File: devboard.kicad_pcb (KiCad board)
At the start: 2 copper layers, 23 x 52 mm, 24 parts, among them J1 USB4105-GF-A, J2 Conn_01x08_Pin, J3 Conn_01x08_Pin, U1 STM32F411CEU6, U2 AP2120N-3.3TRG1, U3 USBLC6-2SC6Y

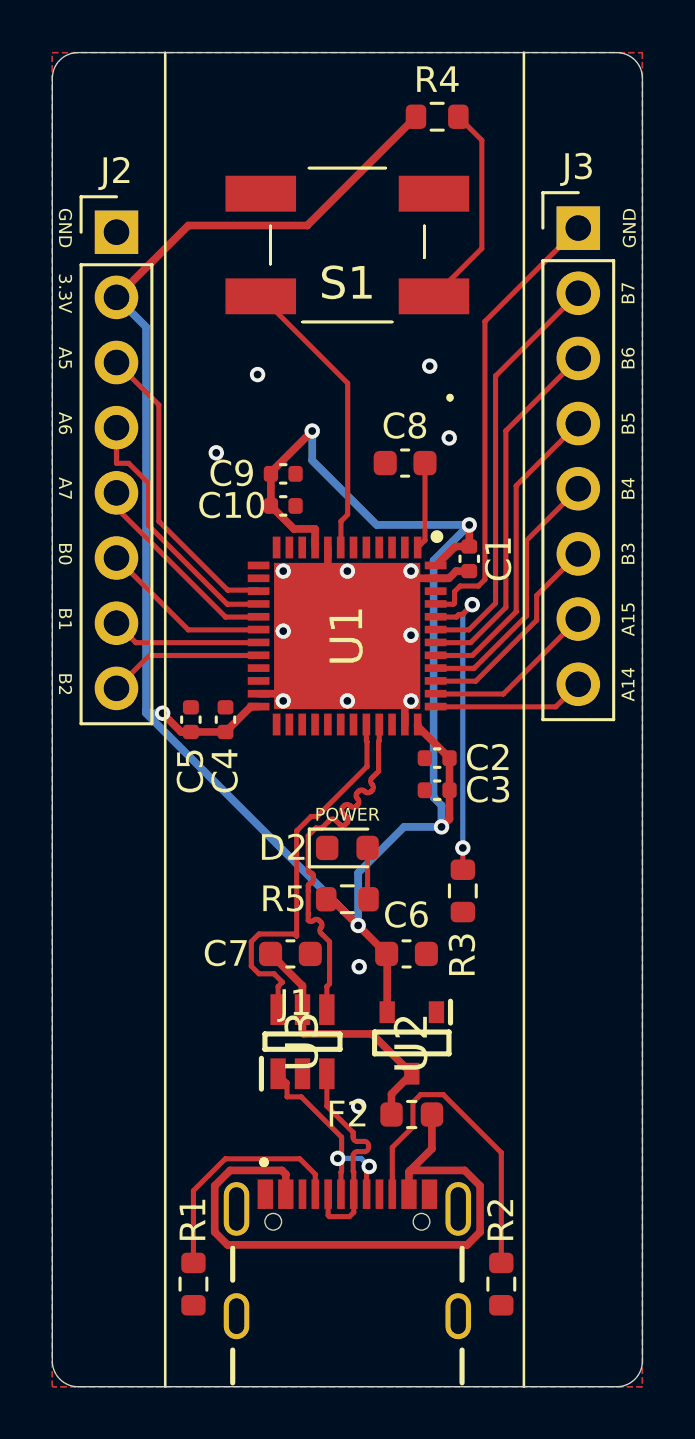
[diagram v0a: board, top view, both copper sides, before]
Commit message: Ground connections fixes
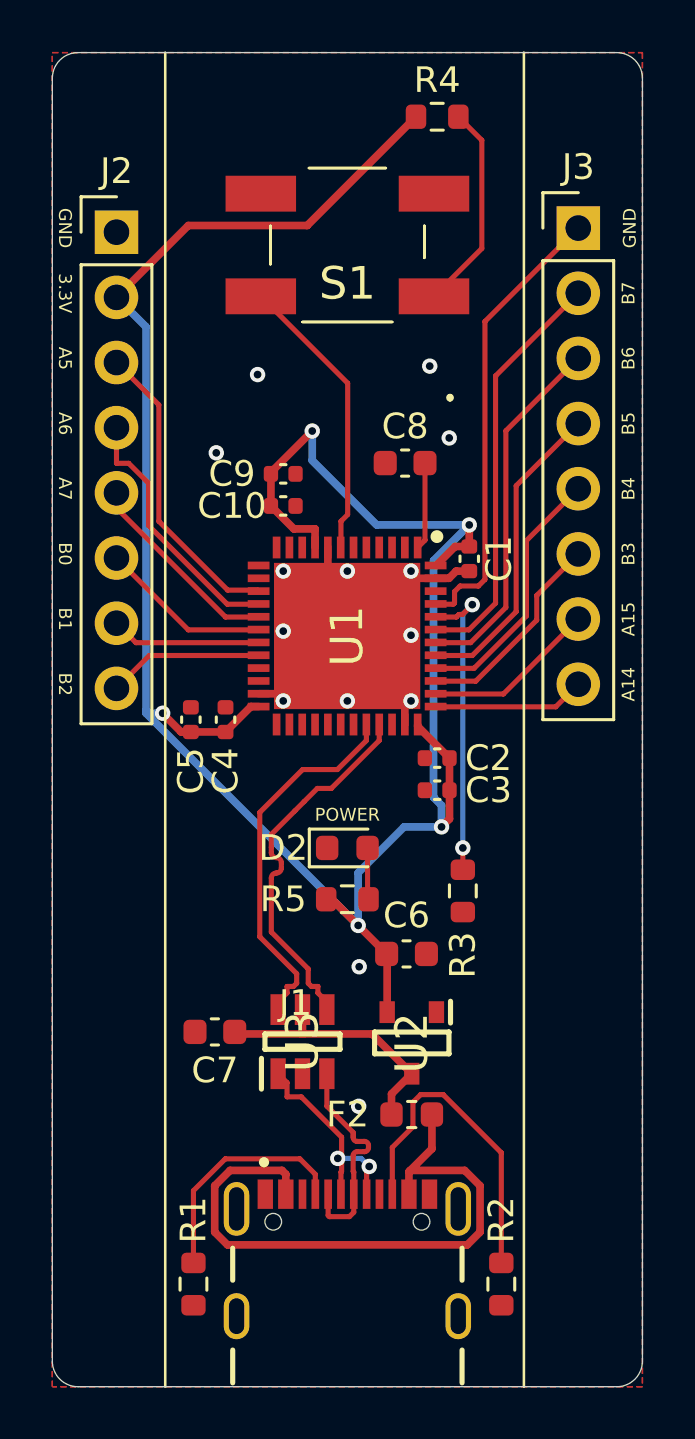
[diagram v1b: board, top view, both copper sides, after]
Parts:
- moved C7 4.23 mm to (108.3, 111.2), turned to 180 degrees

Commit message: Fixed ALL DRC and unconnected errors
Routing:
- net GND: track 18.3 -> 26.6 mm, vias 14 -> 15
- net Net-(F2-Pad2): track 24.7 -> 28.2 mm
- net D-: track 8.65 -> 10.2 mm

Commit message: Fixes
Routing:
- net GND: vias 15 -> 17
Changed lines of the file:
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@@
+	)
+	(via
+		(at 118.19 115.72)
+		(size 0.6)
+		(drill 0.3)
+		(layers "F.Cu" "B.Cu")
+		(free yes)
+		(net 33)
 	)
 	(via
@@
 		(net 33)
 	)
+	(via
+		(at 113.9 112.65)
+		(size 0.6)
+		(drill 0.3)
+		(layers "F.Cu" "B.Cu")
+		(free yes)
+		(net 33)
+	)

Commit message: Fixes
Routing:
- net GND: vias 17 -> 31
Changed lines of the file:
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@@
 			(outputformat 1)
 			(mirror no)
-			(drillshape 1)
+			(drillshape 0)
 			(scaleselection 1)
-			(outputdirectory "")
+			(outputdirectory "gerber/")
 		)
 	)
@@
 	)
 	(via
-		(at 108.39 88.6)
+		(at 114.84 101.6)
+		(size 0.6)
+		(drill 0.3)
+		(layers "F.Cu" "B.Cu")
+		(free yes)
+		(net 33)
+	)
+	(via
+		(at 107.29 88.99)
+		(size 0.6)
+		(drill 0.3)
+		(layers "F.Cu" "B.Cu")
+		(free yes)
+		(net 33)
+	)
+	(via
+		(at 117.97 88.18)
 		(size 0.6)
 		(drill 0.3)
@@
 	)
 	(via
-		(at 116.71 85.22)
+		(at 114.43 80.48)
+		(size 0.6)
+		(drill 0.3)
+		(layers "F.Cu" "B.Cu")
+		(free yes)
+		(net 33)
+	)
+	(via
+		(at 114.26 84.47)
 		(size 0.6)
 		(drill 0.3)
@@
 	)
 	(via
+		(at 107.42 84.54)
+		(size 0.6)
+		(drill 0.3)
+		(layers "F.Cu" "B.Cu")
+		(free yes)
+		(net 33)
+	)
+	(via
+		(at 107.84 97.28)
+		(size 0.6)
+		(drill 0.3)
+		(layers "F.Cu" "B.Cu")
+		(free yes)
+		(net 33)
+	)
+	(via
+		(at 104.27 115.09)
+		(size 0.6)
+		(drill 0.3)
+		(layers "F.Cu" "B.Cu")
+		(free yes)
+		(net 33)
+	)
+	(via
+		(at 123.18 104.09)
+		(size 0.6)
+		(drill 0.3)
+		(layers "F.Cu" "B.Cu")
+		(free yes)
+		(net 33)
+	)
+	(via
 		(at 113.5 120)
 		(size 0.6)
@@
 	)
 	(via
+		(at 122.75 74.59)
+		(size 0.6)
+		(drill 0.3)
+		(layers "F.Cu" "B.Cu")
+		(free yes)
+		(net 33)
+	)
+	(via
+		(at 116.21 105.07)
+		(size 0.6)
+		(drill 0.3)
+		(layers "F.Cu" "B.Cu")
+		(free yes)
+		(net 33)
+	)
+	(via
 		(at 113.5 98.27)
 		(size 0.6)
@@
 	)
 	(via
+		(at 104.78 106.17)
+		(size 0.6)
+		(drill 0.3)
+		(layers "F.Cu" "B.Cu")
+		(free yes)
+		(net 33)
+	)
+	(via
 		(at 113.5 93.21)
 		(size 0.6)
@@
 	)
 	(via
+		(at 111.99 107.47)
+		(size 0.6)
+		(drill 0.3)
+		(layers "F.Cu" "B.Cu")
+		(free yes)
+		(net 33)
+	)
+	(via
 		(at 115.98 95.71)
 		(size 0.6)
@@
 	)
 	(via
+		(at 104.1 74.86)
+		(size 0.6)
+		(drill 0.3)
+		(layers "F.Cu" "B.Cu")
+		(free yes)
+		(net 33)
+	)
+	(via
 		(at 111 98.27)
 		(size 0.6)
@@
 	)
 	(via
+		(at 111.77 103.09)
+		(size 0.6)
+		(drill 0.3)
+		(layers "F.Cu" "B.Cu")
+		(free yes)
+		(net 33)
+	)
+	(via
 		(at 110 85.55)
 		(size 0.6)
@@
 	)
 	(via
-		(at 117.47 88.02)
+		(at 116.09 85.51)
+		(size 0.6)
+		(drill 0.3)
+		(layers "F.Cu" "B.Cu")
+		(free yes)
+		(net 33)
+	)
+	(via
+		(at 122.82 117.58)
 		(size 0.6)
 		(drill 0.3)

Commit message: Fix VBAT
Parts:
- C8: value 2.2 uF -> 100 nF
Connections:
- C8 pad 2: Net-(U1-VBAT) -> +3.3V
- U1 pad 1: Net-(U1-VBAT) -> +3.3V
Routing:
- net Net-(U1-VBAT): track 3.41 -> 0.00 mm
- net +3.3V: track 94.1 -> 97.5 mm, vias 5 -> 6
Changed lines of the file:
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@@
 	(net 34 "Net-(J1-CC2)")
 	(net 35 "unconnected-(J1-SBU1-PadA8)")
-	(net 36 "Net-(U1-VBAT)")
-	(net 37 "Net-(U1-BOOT0)")
-	(net 38 "NRST")
-	(net 39 "B9")
-	(net 40 "unconnected-(U1-PH0-OSC_OUT-Pad6)")
-	(net 41 "unconnected-(U1-PC13-Pad2)")
-	(net 42 "B13")
-	(net 43 "B12")
-	(net 44 "unconnected-(U1-VCAP_1-Pad22)")
-	(net 45 "unconnected-(U1-PC14-OSC32_IN-Pad3)")
-	(net 46 "B10")
-	(net 47 "B14")
-	(net 48 "unconnected-(U1-PH0-OSC_IN-Pad5)")
-	(net 49 "unconnected-(U1-PC15-OSC32_OUT-Pad4)")
-	(net 50 "B15")
-	(net 51 "Net-(D2-A)")
-	(net 52 "Net-(S1-COM_1)")
+	(net 36 "Net-(U1-BOOT0)")
+	(net 37 "NRST")
+	(net 38 "B9")
+	(net 39 "unconnected-(U1-PH0-OSC_OUT-Pad6)")
+	(net 40 "unconnected-(U1-PC13-Pad2)")
+	(net 41 "B13")
+	(net 42 "B12")
+	(net 43 "unconnected-(U1-VCAP_1-Pad22)")
+	(net 44 "unconnected-(U1-PC14-OSC32_IN-Pad3)")
+	(net 45 "B10")
+	(net 46 "B14")
+	(net 47 "unconnected-(U1-PH0-OSC_IN-Pad5)")
+	(net 48 "unconnected-(U1-PC15-OSC32_OUT-Pad4)")
+	(net 49 "B15")
+	(net 50 "Net-(D2-A)")
+	(net 51 "Net-(S1-COM_1)")
 	(footprint "Capacitor_SMD:C_0603_1608Metric"
 		(layer "F.Cu")
@@
 			(layers "F.Cu" "F.Mask" "F.Paste")
 			(roundrect_rratio 0.25)
-			(net 52 "Net-(S1-COM_1)")
+			(net 51 "Net-(S1-COM_1)")
 			(pintype "passive")
 		)
@@
 			)
 		)
-		(property "Value" "2.2 uF"
+		(property "Value" "100 nF"
 			(at 0 1.43 0)
 			(layer "F.Fab")
@@
 			(layers "F.Cu" "F.Mask" "F.Paste")
 			(roundrect_rratio 0.25)
-			(net 36 "Net-(U1-VBAT)")
+			(net 30 "+3.3V")
 			(pintype "passive")
 		)
@@
 			(layers "F.Cu" "F.Mask" "F.Paste")
 			(roundrect_rratio 0.25)
-			(net 51 "Net-(D2-A)")
+			(net 50 "Net-(D2-A)")
 			(pinfunction "A")
 			(pintype "passive")
@@
 			(size 1.4 2.75)
 			(layers "F.Cu" "F.Mask" "F.Paste")
-			(net 52 "Net-(S1-COM_1)")
+			(net 51 "Net-(S1-COM_1)")
 			(pinfunction "COM_1")
 			(pintype "passive")
@@
 			(size 1.4 2.75)
 			(layers "F.Cu" "F.Mask" "F.Paste")
-			(net 38 "NRST")
+			(net 37 "NRST")
 			(pinfunction "COM_2")
 			(pintype "passive")
@@
 			(layers "F.Cu" "F.Mask" "F.Paste")
 			(roundrect_rratio 0.25)
-			(net 51 "Net-(D2-A)")
+			(net 50 "Net-(D2-A)")
 			(pintype "passive")
 		)
@@
 			(size 0.3 0.85)
 			(layers "F.Cu" "F.Mask" "F.Paste")
-			(net 36 "Net-(U1-VBAT)")
+			(net 30 "+3.3V")
 			(pinfunction "VBAT")
 			(pintype "passive")
@@
 			(size 0.3 0.85)
 			(layers "F.Cu" "F.Mask" "F.Paste")
-			(net 41 "unconnected-(U1-PC13-Pad2)")
+			(net 40 "unconnected-(U1-PC13-Pad2)")
 			(pinfunction "PC13")
 			(pintype "passive+no_connect")
@@
 			(size 0.3 0.85)
 			(layers "F.Cu" "F.Mask" "F.Paste")
-			(net 45 "unconnected-(U1-PC14-OSC32_IN-Pad3)")
+			(net 44 "unconnected-(U1-PC14-OSC32_IN-Pad3)")
 			(pinfunction "PC14-OSC32_IN")
 			(pintype "passive+no_connect")
@@
 			(size 0.3 0.85)
 			(layers "F.Cu" "F.Mask" "F.Paste")
-			(net 49 "unconnected-(U1-PC15-OSC32_OUT-Pad4)")
+			(net 48 "unconnected-(U1-PC15-OSC32_OUT-Pad4)")
 			(pinfunction "PC15-OSC32_OUT")
 			(pintype "passive+no_connect")
@@
 			(size 0.3 0.85)
 			(layers "F.Cu" "F.Mask" "F.Paste")
-			(net 48 "unconnected-(U1-PH0-OSC_IN-Pad5)")
+			(net 47 "unconnected-(U1-PH0-OSC_IN-Pad5)")
 			(pinfunction "PH0-OSC_IN")
 			(pintype "passive+no_connect")
@@
 			(size 0.3 0.85)
 			(layers "F.Cu" "F.Mask" "F.Paste")
-			(net 40 "unconnected-(U1-PH0-OSC_OUT-Pad6)")
+			(net 39 "unconnected-(U1-PH0-OSC_OUT-Pad6)")
 			(pinfunction "PH0-OSC_OUT")
 			(pintype "passive+no_connect")
@@
 			(size 0.3 0.85)
 			(layers "F.Cu" "F.Mask" "F.Paste")
-			(net 38 "NRST")
+			(net 37 "NRST")
 			(pinfunction "NRST")
 			(pintype "passive")
@@
 			(size 0.3 0.85)
 			(layers "F.Cu" "F.Mask" "F.Paste")
-			(net 46 "B10")
+			(net 45 "B10")
 			(pinfunction "PB10")
 			(pintype "passive+no_connect")
@@
 			(size 0.3 0.85)
 			(layers "F.Cu" "F.Mask" "F.Paste")
-			(net 44 "unconnected-(U1-VCAP_1-Pad22)")
+			(net 43 "unconnected-(U1-VCAP_1-Pad22)")
 			(pinfunction "VCAP_1")
 			(pintype "passive+no_connect")
@@
 			(size 0.3 0.85)
 			(layers "F.Cu" "F.Mask" "F.Paste")
-			(net 43 "B12")
+			(net 42 "B12")
 			(pinfunction "PB12")
 			(pintype "passive+no_connect")
@@
 			(size 0.3 0.85)
 			(layers "F.Cu" "F.Mask" "F.Paste")
-			(net 42 "B13")
+			(net 41 "B13")
 			(pinfunction "PB13")
 			(pintype "passive+no_connect")
@@
 			(size 0.3 0.85)
 			(layers "F.Cu" "F.Mask" "F.Paste")
-			(net 47 "B14")
+			(net 46 "B14")
 			(pinfunction "PB14")
 			(pintype "passive+no_connect")
@@
 			(size 0.3 0.85)
 			(layers "F.Cu" "F.Mask" "F.Paste")
-			(net 50 "B15")
+			(net 49 "B15")
 			(pinfunction "PB15")
 			(pintype "passive+no_connect")
@@
 			(size 0.3 0.85)
 			(layers "F.Cu" "F.Mask" "F.Paste")
-			(net 37 "Net-(U1-BOOT0)")
+			(net 36 "Net-(U1-BOOT0)")
 			(pinfunction "BOOT0")
 			(pintype "passive")
@@
 			(size 0.3 0.85)
 			(layers "F.Cu" "F.Mask" "F.Paste")
-			(net 39 "B9")
+			(net 38 "B9")
 			(pinfunction "PB9")
 			(pintype "passive+no_connect")
@@
 			(layers "F.Cu" "F.Mask" "F.Paste")
 			(roundrect_rratio 0.25)
-			(net 37 "Net-(U1-BOOT0)")
+			(net 36 "Net-(U1-BOOT0)")
 			(pintype "passive")
 		)
@@
 	)
 	(segment
+		(start 116.525 92.005)
+		(end 116.24 92.29)
+		(width 0.3)
+		(layer "F.Cu")
+		(net 30)
+	)
+	(segment
 		(start 115.05 108.15)
 		(end 115.03 108.13)
@@
 	)
 	(segment
+		(start 116.525 89)
+		(end 116.525 91.4)
+		(width 0.3)
+		(layer "F.Cu")
+		(net 30)
+	)
+	(segment
+		(start 116.525 91.4)
+		(end 116.525 92.005)
+		(width 0.3)
+		(layer "F.Cu")
+		(net 30)
+	)
+	(segment
 		(start 115.05 110.4)
 		(end 115.05 108.15)
@@
 		(net 30)
 	)
+	(via
+		(at 116.525 91.4)
+		(size 0.6)
+		(drill 0.3)
+		(layers "F.Cu" "B.Cu")
+		(net 30)
+	)
 	(segment
 		(start 106.3 98.75)
@@
 	)
 	(segment
-		(start 116.525 92.005)
-		(end 116.24 92.29)
-		(width 0.2)
-		(layer "F.Cu")
-		(net 36)
-	)
-	(segment
-		(start 116.525 89)
-		(end 116.525 92.005)
-		(width 0.2)
-		(layer "F.Cu")
-		(net 36)
-	)
-	(segment
 		(start 117.85 94.9)
 		(end 117.75 95)
 		(width 0.2)
 		(layer "F.Cu")
-		(net 37)
+		(net 36)
 	)
 	(segment
@@
 		(width 0.2)
 		(layer "F.Cu")
-		(net 37)
+		(net 36)
 	)
 	(segment
@@
 		(width 0.2)
 		(layer "F.Cu")
-		(net 37)
+		(net 36)
 	)
 	(segment
@@
 		(width 0.2)
 		(layer "F.Cu")
-		(net 37)
+		(net 36)
 	)
 	(segment
@@
 		(width 0.2)
 		(layer "F.Cu")
-		(net 37)
+		(net 36)
 	)
 	(via
@@
 		(drill 0.3)
 		(layers "F.Cu" "B.Cu")
-		(net 37)
+		(net 36)
 	)
 	(via
@@
 		(drill 0.3)
 		(layers "F.Cu" "B.Cu")
-		(net 37)
+		(net 36)
 	)
 	(segment
@@
 		(width 0.2)
 		(layer "B.Cu")
-		(net 37)
+		(net 36)
 	)
 	(segment
@@
 		(width 0.2)
 		(layer "B.Cu")
-		(net 37)
+		(net 36)
 	)
 	(segment
@@
 		(width 0.2)
 		(layer "F.Cu")
-		(net 38)
+		(net 37)
 	)
 	(segment
@@
 		(width 0.2)
 		(layer "F.Cu")
-		(net 38)
+		(net 37)
 	)
 	(segment
@@
 		(width 0.2)
 		(layer "F.Cu")
-		(net 38)
+		(net 37)
 	)
 	(segment
@@
 		(width 0.2)
 		(layer "F.Cu")
-		(net 38)
+		(net 37)
 	)
 	(segment
@@
 		(width 0.2)
 		(layer "F.Cu")
-		(net 51)
+		(net 50)
 	)
 	(segment
@@
 		(width 0.2)
 		(layer "F.Cu")
-		(net 51)
+		(net 50)
 	)
 	(segment
@@
 		(width 0.2)
 		(layer "F.Cu")
-		(net 52)
+		(net 51)
 	)
 	(segment
@@
 		(width 0.2)
 		(layer "F.Cu")
-		(net 52)
+		(net 51)
 	)
 	(segment
@@
 		(width 0.2)
 		(layer "F.Cu")
-		(net 52)
+		(net 51)
 	)
 	(zone

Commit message: Fixes
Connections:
- U3 pad 1: D+ -> D-
- U3 pad 3: D- -> D+
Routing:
- net Net-(F2-Pad2): track 28.2 -> 10.2 mm
- net D-: track 10.2 -> 8.09 mm
- net D+: track 8.64 -> 8.05 mm, vias 2 -> 0

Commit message: Fixes
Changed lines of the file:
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@@
-		(net 33)
-		(net_name "GND")
-		(layer "F.Cu")
-		(hatch edge 0.5)
-		(connect_pads
-			(clearance 0.5)
-		)
-		(min_thickness 0.25)
-		(filled_areas_thickness no)
-		(fill yes
-			(thermal_gap 0.5)
-			(thermal_bridge_width 0.5)
-		)
-		(polygon
-			(pts
-				(xy 102 73) (xy 125 73) (xy 125 125) (xy 102 125)
-			)
-		)
-	)
-	(zone
 		(net 33)
 		(net_name "GND")

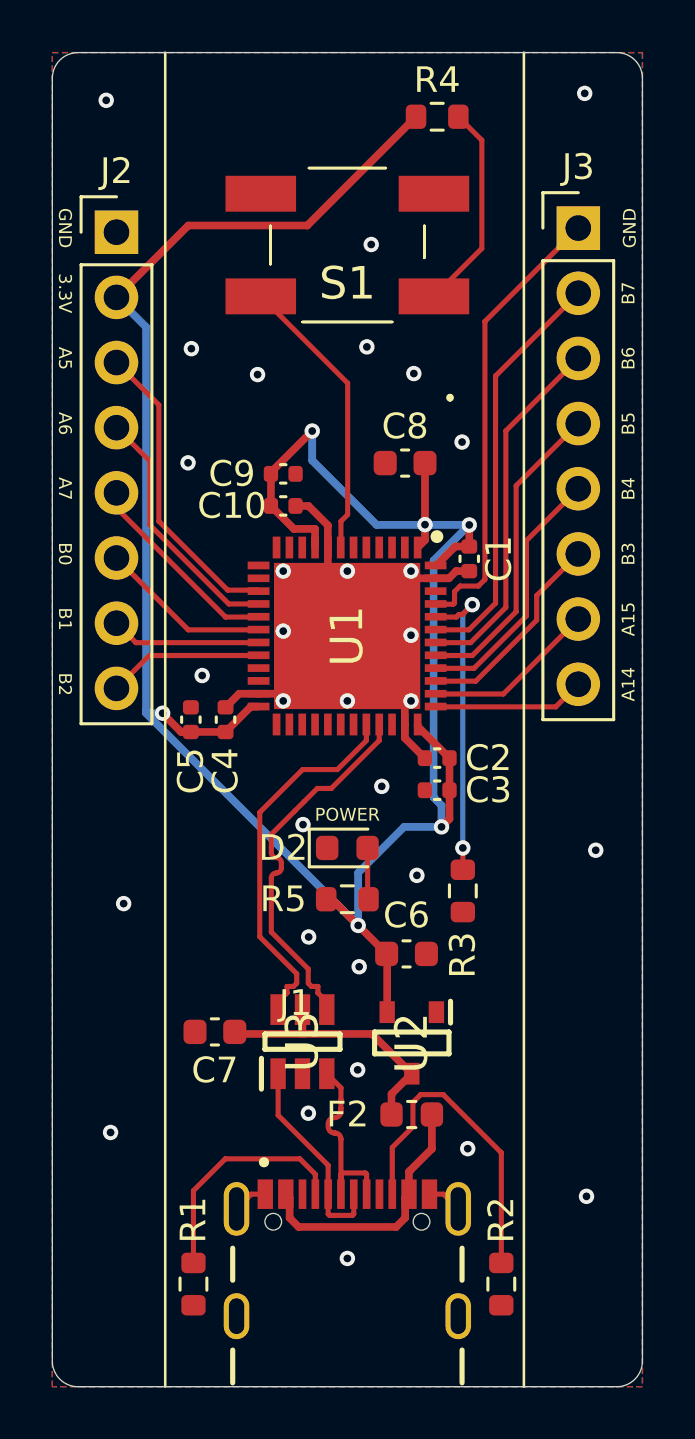
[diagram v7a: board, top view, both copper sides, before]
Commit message: Increase PWR LED resistence value + better silkscreen placement
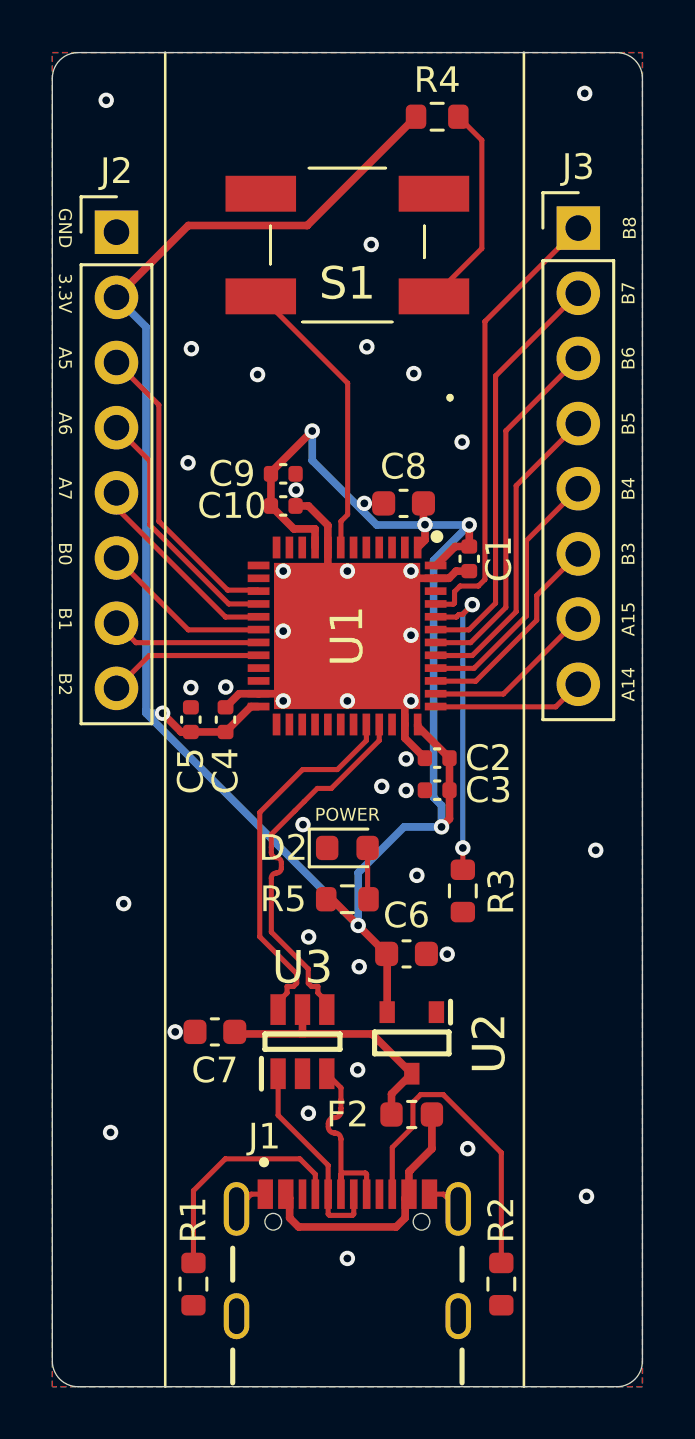
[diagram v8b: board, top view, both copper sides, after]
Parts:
- moved C8 1.57 mm to (115.7, 90.6)
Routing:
- net +3.3V: track 97.5 -> 95.9 mm
- net GND: vias 31 -> 38
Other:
- board text added: "B8"
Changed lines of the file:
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@@
 			(crossoutdnponfab yes)
 			(subtractmaskfromsilk no)
-			(outputformat 4)
+			(outputformat 1)
 			(mirror no)
 			(drillshape 0)
@@
 	(footprint "Capacitor_SMD:C_0603_1608Metric"
 		(layer "F.Cu")
-		(at 115.75 89)
+		(at 115.69 90.57)
 		(descr "Capacitor SMD 0603 (1608 Metric), square (rectangular) end terminal, IPC-7351 nominal, (Body size source: IPC-SM-782 page 76, https://www.pcb-3d.com/wordpress/wp-content/uploads/ipc-sm-782a_amendment_1_and_2.pdf), generated with kicad-footprint-generator")
 		(tags "capacitor")
@@
 		(tags "Diode")
 		(property "Reference" "U3"
-			(at 0 0 90)
+			(at 2.89 0 180)
 			(layer "F.SilkS")
 			(effects
@@
 		)
 		(fp_text user "${REFERENCE}"
-			(at 0 0 90)
+			(at 3.09 -2.66 90)
 			(layer "F.Fab")
 			(effects
@@
 		(tags "Integrated Circuit")
 		(property "Reference" "U2"
-			(at 0 0 270)
+			(at 0.02 -3.02 270)
 			(layer "F.SilkS")
 			(effects
@@
 		)
 		(fp_text user "${REFERENCE}"
-			(at 0 0 270)
+			(at -1.06 -3.02 270)
 			(layer "F.Fab")
 			(effects
@@
 		(tags "resistor")
 		(property "Reference" "R3"
-			(at -2.5 0 90)
+			(at -0.025 1.5 90)
 			(layer "F.SilkS")
 			(effects
@@
 		(at 113.5 122.25)
 		(property "Reference" "J1"
-			(at -2.025 -12.205 0)
+			(at -3.23 -7 0)
 			(layer "F.SilkS")
 			(effects
@@
 		)
 	)
-	(gr_text "GND\n"
+	(gr_text "B8\n"
 		(at 124.8 79.84 90)
 		(layer "F.SilkS")
@@
 	)
 	(segment
+		(start 116.465 90.57)
+		(end 116.465 91.34)
+		(width 0.3)
+		(layer "F.Cu")
+		(net 30)
+	)
+	(segment
 		(start 112.24 91.565)
 		(end 111.415 91.565)
@@
 	)
 	(segment
+		(start 116.465 91.34)
+		(end 116.525 91.4)
+		(width 0.3)
+		(layer "F.Cu")
+		(net 30)
+	)
+	(segment
 		(start 112.675 106)
 		(end 112.9 106)
@@
 	)
 	(segment
-		(start 116.525 89)
-		(end 116.525 91.4)
-		(width 0.3)
-		(layer "F.Cu")
-		(net 30)
-	)
-	(segment
 		(start 116.525 91.4)
 		(end 116.525 92.005)
@@
 	)
 	(via
+		(at 108.76 97.73)
+		(size 0.6)
+		(drill 0.3)
+		(layers "F.Cu" "B.Cu")
+		(free yes)
+		(net 33)
+	)
+	(via
 		(at 118.19 115.72)
 		(size 0.6)
@@
 	)
 	(via
+		(at 115.79 101.76)
+		(size 0.6)
+		(drill 0.3)
+		(layers "F.Cu" "B.Cu")
+		(free yes)
+		(net 33)
+	)
+	(via
+		(at 114.16 90.57)
+		(size 0.6)
+		(drill 0.3)
+		(layers "F.Cu" "B.Cu")
+		(free yes)
+		(net 33)
+	)
+	(via
 		(at 114.26 84.47)
 		(size 0.6)
@@
 	)
 	(via
-		(at 107.84 97.28)
+		(at 117.39 108.14)
+		(size 0.6)
+		(drill 0.3)
+		(layers "F.Cu" "B.Cu")
+		(free yes)
+		(net 33)
+	)
+	(via
+		(at 107.4 97.75)
 		(size 0.6)
 		(drill 0.3)
@@
 	)
 	(via
+		(at 111.5 90.05)
+		(size 0.6)
+		(drill 0.3)
+		(layers "F.Cu" "B.Cu")
+		(free yes)
+		(net 33)
+	)
+	(via
 		(at 123.18 104.09)
 		(size 0.6)
@@
 	)
 	(via
+		(at 115.79 100.53)
+		(size 0.6)
+		(drill 0.3)
+		(layers "F.Cu" "B.Cu")
+		(free yes)
+		(net 33)
+	)
+	(via
 		(at 111.99 107.47)
 		(size 0.6)
@@
 		(size 0.6)
 		(drill 0.3)
+		(layers "F.Cu" "B.Cu")
+		(free yes)
+		(net 33)
+	)
+	(via
+		(at 106.79 111.17)
+		(size 0.6)
+		(drill 0.3)
